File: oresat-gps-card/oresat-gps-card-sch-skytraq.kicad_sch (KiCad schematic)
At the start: 11 parts, among them U23 ORION-B16

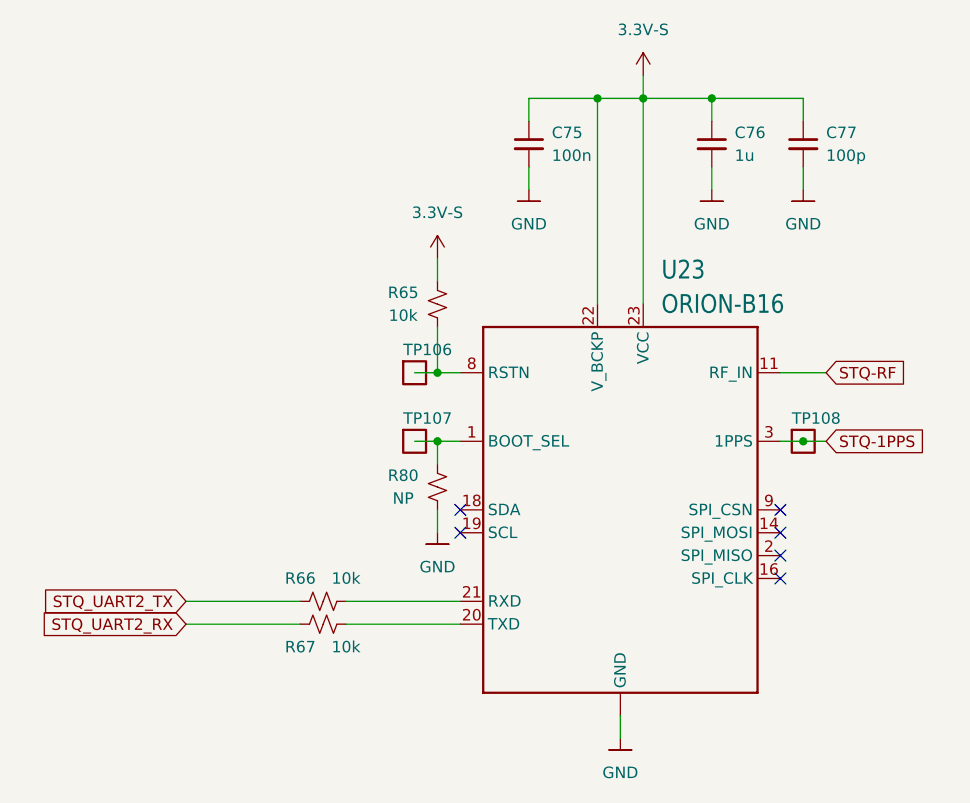
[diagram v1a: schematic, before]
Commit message: Quick GPS card design review changes
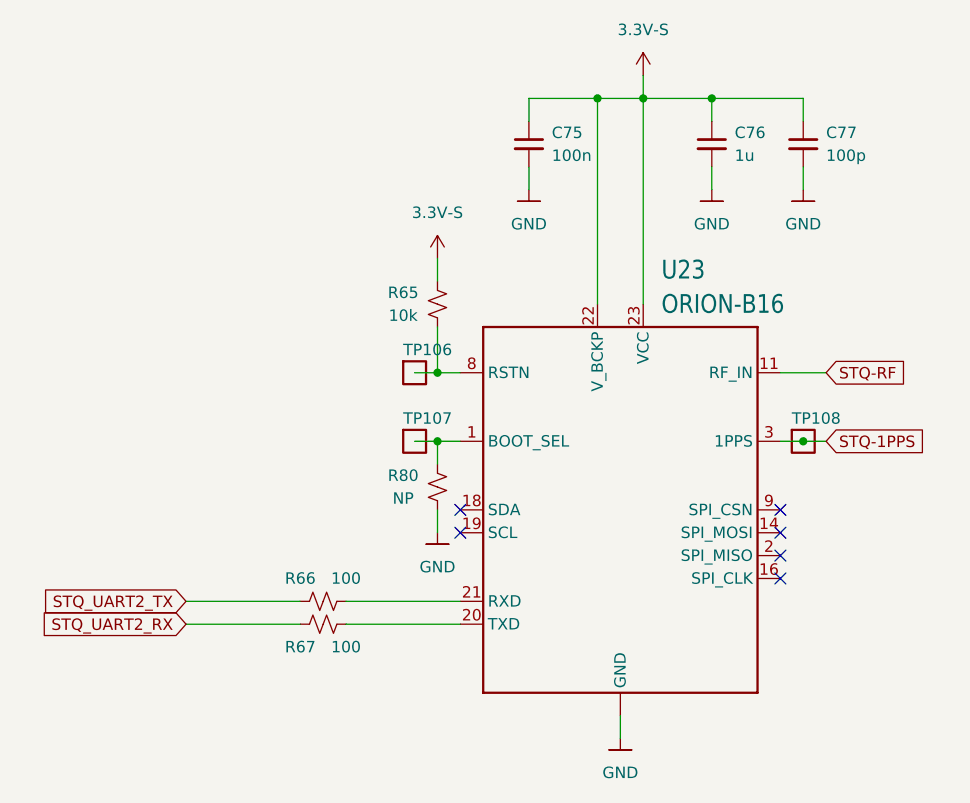
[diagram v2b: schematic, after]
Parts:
- R66, R67: value 10k -> 100
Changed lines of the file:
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@@
   (symbol (lib_id "OreSat-Power:GND") (at 226.06 99.06 0) (unit 1)
     (in_bom yes) (on_board yes) (fields_autoplaced)
-    (property "Reference" "#GND?" (id 0) (at 226.06 105.41 0)
+    (property "Reference" "#GND0222" (id 0) (at 226.06 105.41 0)
       (effects (font (size 1.27 1.27)) hide)
     )
@@
   (symbol (lib_id "OreSat-Power:GND") (at 205.74 99.06 0) (unit 1)
     (in_bom yes) (on_board yes) (fields_autoplaced)
-    (property "Reference" "#GND?" (id 0) (at 205.74 105.41 0)
+    (property "Reference" "#GND0221" (id 0) (at 205.74 105.41 0)
       (effects (font (size 1.27 1.27)) hide)
     )
@@
   (symbol (lib_id "OreSat-Power:GND") (at 215.9 160.02 0) (unit 1)
     (in_bom yes) (on_board yes) (fields_autoplaced)
-    (property "Reference" "#GND?" (id 0) (at 215.9 166.37 0)
+    (property "Reference" "#GND0225" (id 0) (at 215.9 166.37 0)
       (effects (font (size 1.27 1.27)) hide)
     )
@@
     (in_bom yes) (on_board yes)
     (property "Reference" "R67" (id 0) (at 180.34 149.86 90))
-    (property "Value" "10k" (id 1) (at 185.42 149.86 90))
+    (property "Value" "100" (id 1) (at 185.42 149.86 90))
     (property "Footprint" "Resistor_SMD:R_0603_1608Metric" (id 2) (at 182.88 147.32 0)
       (effects (font (size 1.27 1.27)) hide)
@@
   (symbol (lib_id "gps-power:3.3V-S") (at 218.44 86.36 0) (unit 1)
     (in_bom no) (on_board no) (fields_autoplaced)
-    (property "Reference" "#3V3-S?" (id 0) (at 218.44 81.28 0)
+    (property "Reference" "#3V3-S0102" (id 0) (at 218.44 81.28 0)
       (effects (font (size 1.27 1.27)) hide)
     )
@@
   (symbol (lib_id "OreSat-Power:GND") (at 195.58 137.16 0) (unit 1)
     (in_bom yes) (on_board yes) (fields_autoplaced)
-    (property "Reference" "#GND?" (id 0) (at 195.58 143.51 0)
+    (property "Reference" "#GND0224" (id 0) (at 195.58 143.51 0)
       (effects (font (size 1.27 1.27)) hide)
     )
@@
     (in_bom yes) (on_board yes)
     (property "Reference" "R66" (id 0) (at 180.34 142.24 90))
-    (property "Value" "10k" (id 1) (at 185.42 142.24 90))
+    (property "Value" "100" (id 1) (at 185.42 142.24 90))
     (property "Footprint" "Resistor_SMD:R_0603_1608Metric" (id 2) (at 182.88 144.78 0)
       (effects (font (size 1.27 1.27)) hide)
@@
   (symbol (lib_id "OreSat-Power:GND") (at 236.22 99.06 0) (unit 1)
     (in_bom yes) (on_board yes) (fields_autoplaced)
-    (property "Reference" "#GND?" (id 0) (at 236.22 105.41 0)
+    (property "Reference" "#GND0223" (id 0) (at 236.22 105.41 0)
       (effects (font (size 1.27 1.27)) hide)
     )
@@
   (symbol (lib_id "gps-power:3.3V-S") (at 195.58 106.68 0) (unit 1)
     (in_bom no) (on_board no) (fields_autoplaced)
-    (property "Reference" "#3V3-S?" (id 0) (at 195.58 101.6 0)
-      (effects (font (size 1.27 1.27)) hide)
-    )
+    (property "Reference" "#3V3-S0103" (id 0) (at 195.58 101.6 0)
+      (effects (font (size 1.27 1.27)) hide)
+    )

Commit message: Updated GPS card with changes from C3 and notes. Fixed library issues
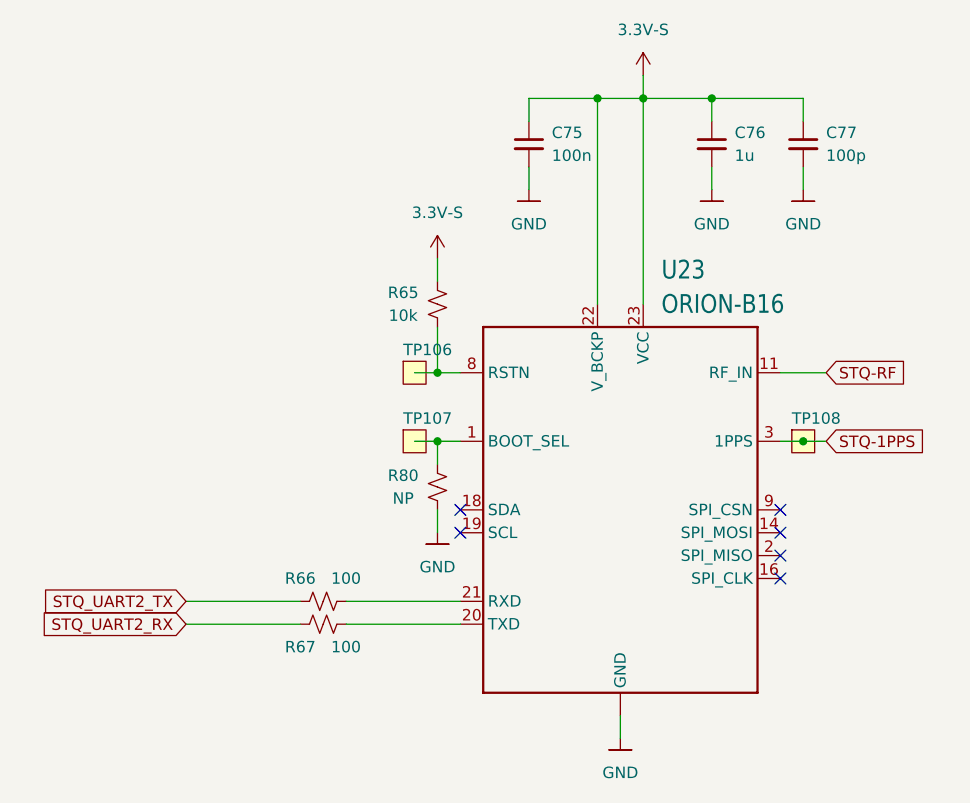
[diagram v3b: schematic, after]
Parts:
- TP106, TP107, TP108: value Test-Point -> 1x01; footprint OreSat-TestPoint:1X01 -> oresat-misc:TestPoint-0.75mm-th; symbol OreSat-TestPoint:Test-Point -> oresat-misc:Test-Point-0.75mm-th
- U23: symbol U-SkyTraq-ORION-B16-gps-receiver:ORION-B16 -> oresat-ics:ORION-B16

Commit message: Cleaned up ERC and DRC errors on GPS card
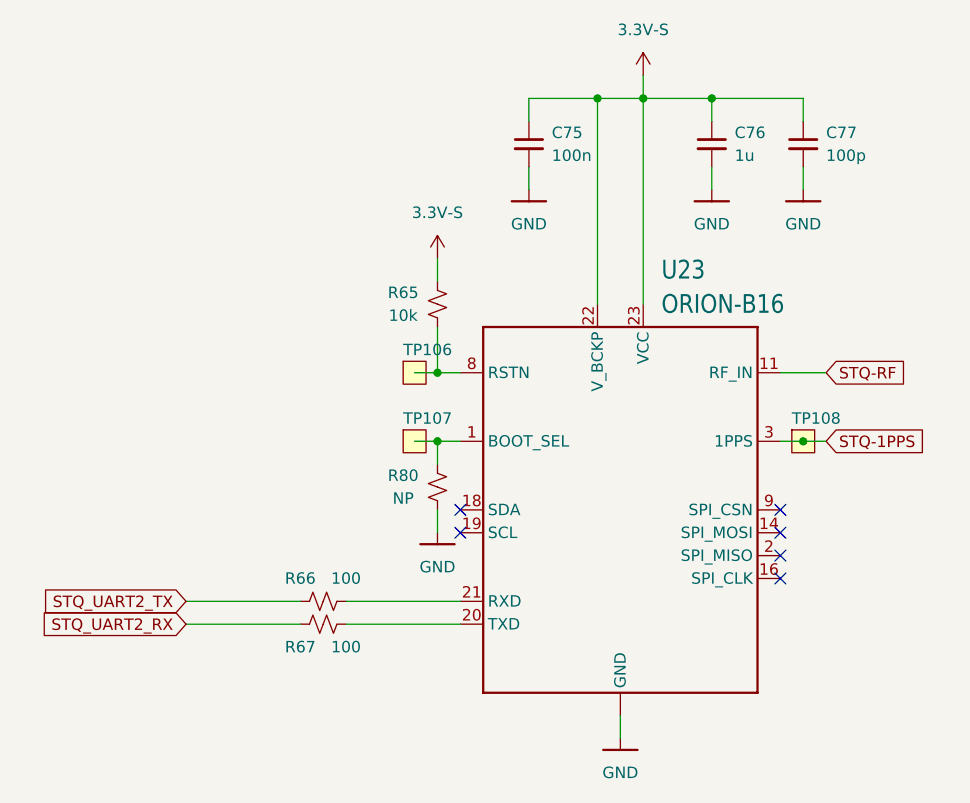
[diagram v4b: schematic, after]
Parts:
- U23: footprint oresat-footprints:U-SkyTraq-ORION-B16 -> oresat-ics:U-SkyTraq-ORION-B16
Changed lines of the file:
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@@
       (effects (font (size 2.0828 1.7703)) (justify left))
     )
-    (property "Footprint" "oresat-footprints:U-SkyTraq-ORION-B16" (at 215.9 134.62 0)
+    (property "Footprint" "oresat-ics:U-SkyTraq-ORION-B16" (at 215.9 134.62 0)
       (effects (font (size 1.27 1.27)) hide)
     )

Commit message: Updated KiCAD 8, updated schematic sheet info, polished some schematic things, and made DNP parts DNP.
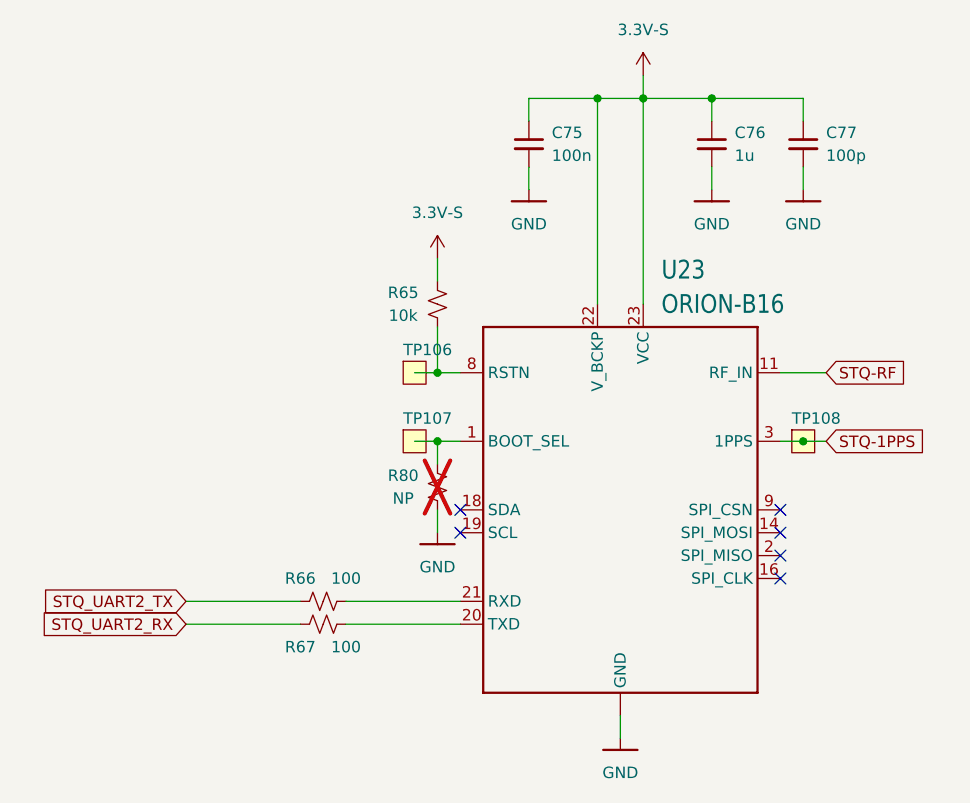
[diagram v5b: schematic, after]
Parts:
- R80: now not fitted; now left out of the parts list
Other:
- title: (none) -> OreSat GPS Card

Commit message: updated symbols and started new 2771 symbol
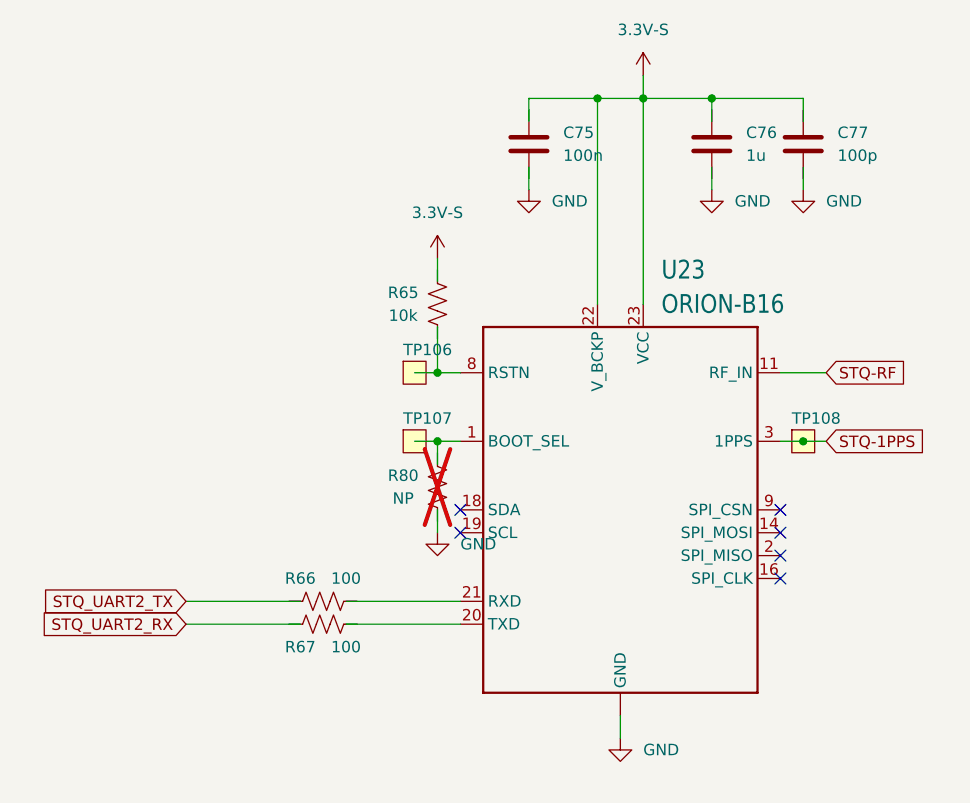
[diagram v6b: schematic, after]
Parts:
- C75, C76, C77: symbol Device:C_Small -> Device:C
- R65, R66, R67: symbol Device:R_Small_US -> Device:R_US
- R80: symbol Device:R_Small_US -> Device:R_US; now in the parts list
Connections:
- net 3.3V-S: no longer C75.1, C76.1, C77.1, R65.1
- net GND: no longer C75.2, C76.2, C77.2, R80.2
- net STQ_UART2_RX: no longer R67.1
- net STQ_UART2_TX: no longer R66.1
- net at TP106.1, U23.8 (RSTN): no longer R65.2
- net at TP107.1, U23.1 (BOOT_SEL): no longer R80.1
- net at R67.2: no longer U23.20 (TXD)
- net at U23.21 (RXD): no longer R66.2
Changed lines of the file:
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@@
 (kicad_sch
-	(version 20231120)
+	(version 20250114)
 	(generator "eeschema")
-	(generator_version "8.0")
+	(generator_version "9.0")
 	(paper "B")
 	(title_block
@@
 	)
 	(symbol
-		(lib_id "oresat-power:GND")
+		(lib_id "power:GND")
 		(at 226.06 99.06 0)
 		(unit 1)
@@
 		)
 		(property "Value" "GND"
-			(at 226.06 102.87 0)
-			(effects
-				(font
-					(size 1.27 1.27)
-				)
+			(at 228.6 100.3299 0)
+			(effects
+				(font
+					(size 1.27 1.27)
+				)
+				(justify left)
 			)
 		)
@@
 			)
 		)
-		(property "Description" ""
+		(property "Description" "Power symbol creates a global label with name \"GND\" , ground"
 			(at 226.06 99.06 0)
 			(effects
@@
 	)
 	(symbol
-		(lib_id "oresat-power:GND")
+		(lib_id "power:GND")
 		(at 205.74 99.06 0)
 		(unit 1)
@@
 		)
 		(property "Value" "GND"
-			(at 205.74 102.87 0)
-			(effects
-				(font
-					(size 1.27 1.27)
-				)
+			(at 208.28 100.3299 0)
+			(effects
+				(font
+					(size 1.27 1.27)
+				)
+				(justify left)
 			)
 		)
@@
 			)
 		)
-		(property "Description" ""
+		(property "Description" "Power symbol creates a global label with name \"GND\" , ground"
 			(at 205.74 99.06 0)
 			(effects
@@
 	)
 	(symbol
-		(lib_id "Device:R_Small_US")
+		(lib_id "Device:R_US")
 		(at 195.58 111.76 0)
 		(unit 1)
@@
 		)
 		(property "Footprint" "Resistor_SMD:R_0603_1608Metric"
-			(at 195.58 111.76 0)
+			(at 196.596 112.014 90)
 			(effects
 				(font
@@
 			)
 		)
-		(property "Description" ""
+		(property "Description" "Resistor, US symbol"
 			(at 195.58 111.76 0)
 			(effects
@@
 	)
 	(symbol
-		(lib_id "Device:C_Small")
+		(lib_id "Device:C")
 		(at 226.06 93.98 0)
 		(unit 1)
@@
 		(fields_autoplaced yes)
 		(property "Reference" "C76"
-			(at 228.6 92.7162 0)
+			(at 229.87 92.7099 0)
 			(effects
 				(font
@@
 		)
 		(property "Value" "1u"
-			(at 228.6 95.2562 0)
+			(at 229.87 95.2499 0)
 			(effects
 				(font
@@
 		)
 		(property "Footprint" "Capacitor_SMD:C_0603_1608Metric"
-			(at 226.06 93.98 0)
+			(at 227.0252 97.79 0)
 			(effects
 				(font
@@
 			)
 		)
-		(property "Description" ""
+		(property "Description" "Unpolarized capacitor"
 			(at 226.06 93.98 0)
 			(effects
@@
 	)
 	(symbol
-		(lib_id "oresat-power:GND")
+		(lib_id "power:GND")
 		(at 215.9 160.02 0)
 		(unit 1)
@@
 		)
 		(property "Value" "GND"
-			(at 215.9 163.83 0)
-			(effects
-				(font
-					(size 1.27 1.27)
-				)
+			(at 218.44 161.2899 0)
+			(effects
+				(font
+					(size 1.27 1.27)
+				)
+				(justify left)
 			)
 		)
@@
 			)
 		)
-		(property "Description" ""
+		(property "Description" "Power symbol creates a global label with name \"GND\" , ground"
 			(at 215.9 160.02 0)
 			(effects
@@
 	)
 	(symbol
-		(lib_id "Device:C_Small")
+		(lib_id "Device:C")
 		(at 205.74 93.98 0)
 		(unit 1)
@@
 		(fields_autoplaced yes)
 		(property "Reference" "C75"
-			(at 208.28 92.7162 0)
+			(at 209.55 92.7099 0)
 			(effects
 				(font
@@
 		)
 		(property "Value" "100n"
-			(at 208.28 95.2562 0)
+			(at 209.55 95.2499 0)
 			(effects
 				(font
@@
 		)
 		(property "Footprint" "Capacitor_SMD:C_0603_1608Metric"
-			(at 205.74 93.98 0)
+			(at 206.7052 97.79 0)
 			(effects
 				(font
@@
 			)
 		)
-		(property "Description" ""
+		(property "Description" "Unpolarized capacitor"
 			(at 205.74 93.98 0)
 			(effects
@@
 	)
 	(symbol
-		(lib_id "Device:R_Small_US")
+		(lib_id "Device:R_US")
 		(at 182.88 147.32 90)
 		(unit 1)
@@
 		)
 		(property "Footprint" "Resistor_SMD:R_0603_1608Metric"
-			(at 182.88 147.32 0)
+			(at 183.134 146.304 90)
 			(effects
 				(font
@@
 			)
 		)
-		(property "Description" ""
+		(property "Description" "Resistor, US symbol"
 			(at 182.88 147.32 0)
 			(effects
@@
 	)
 	(symbol
-		(lib_id "Device:C_Small")
+		(lib_id "Device:C")
 		(at 236.22 93.98 0)
 		(unit 1)
@@
 		(fields_autoplaced yes)
 		(property "Reference" "C77"
-			(at 238.76 92.7162 0)
+			(at 240.03 92.7099 0)
 			(effects
 				(font
@@
 		)
 		(property "Value" "100p"
-			(at 238.76 95.2562 0)
+			(at 240.03 95.2499 0)
 			(effects
 				(font
@@
 		)
 		(property "Footprint" "Capacitor_SMD:C_0603_1608Metric"
-			(at 236.22 93.98 0)
+			(at 237.1852 97.79 0)
 			(effects
 				(font
@@
 			)
 		)
-		(property "Description" ""
+		(property "Description" "Unpolarized capacitor"
 			(at 236.22 93.98 0)
 			(effects
@@
 	)
 	(symbol
-		(lib_id "oresat-power:GND")
+		(lib_id "power:GND")
 		(at 195.58 137.16 0)
 		(unit 1)
@@
 		)
 		(property "Value" "GND"
-			(at 195.58 140.97 0)
-			(effects
-				(font
-					(size 1.27 1.27)
-				)
+			(at 198.12 138.4299 0)
+			(effects
+				(font
+					(size 1.27 1.27)
+				)
+				(justify left)
 			)
 		)
@@
 			)
 		)
-		(property "Description" ""
+		(property "Description" "Power symbol creates a global label with name \"GND\" , ground"
 			(at 195.58 137.16 0)
 			(effects
@@
 	)
 	(symbol
-		(lib_id "Device:R_Small_US")
+		(lib_id "Device:R_US")
 		(at 182.88 144.78 90)
 		(unit 1)
@@
 		)
 		(property "Footprint" "Resistor_SMD:R_0603_1608Metric"
-			(at 182.88 144.78 0)
+			(at 183.134 143.764 90)
 			(effects
 				(font
@@
 			)
 		)
-		(property "Description" ""
+		(property "Description" "Resistor, US symbol"
 			(at 182.88 144.78 0)
 			(effects
@@
 	)
 	(symbol
-		(lib_id "oresat-power:GND")
+		(lib_id "power:GND")
 		(at 236.22 99.06 0)
 		(unit 1)
@@
 		)
 		(property "Value" "GND"
-			(at 236.22 102.87 0)
-			(effects
-				(font
-					(size 1.27 1.27)
-				)
+			(at 238.76 100.3299 0)
+			(effects
+				(font
+					(size 1.27 1.27)
+				)
+				(justify left)
 			)
 		)
@@
 			)
 		)
-		(property "Description" ""
+		(property "Description" "Power symbol creates a global label with name \"GND\" , ground"
 			(at 236.22 99.06 0)
 			(effects
@@
 	)
 	(symbol
-		(lib_id "Device:R_Small_US")
+		(lib_id "Device:R_US")
 		(at 195.58 132.08 0)
 		(unit 1)
 		(exclude_from_sim no)
-		(in_bom no)
+		(in_bom yes)
 		(on_board yes)
 		(dnp yes)
@@
 		)
 		(property "Footprint" "Resistor_SMD:R_0603_1608Metric"
-			(at 195.58 132.08 0)
+			(at 196.596 132.334 90)
 			(effects
 				(font
@@
 			)
 		)
-		(property "Description" ""
+		(property "Description" "Resistor, US symbol"
 			(at 195.58 132.08 0)
 			(effects

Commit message: Routine Push
Various small changes made
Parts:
- removed TP106, TP107, TP108: 1x01, oresat-misc:TestPoint-0.75mm-th, symbol oresat-misc:Test-Point-0.75mm-th
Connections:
- net 3.3V-S: now also C75.1, C76.1, C77.1
- net GND: now also C75.2, C76.2, C77.2
- net at U23.8 (RSTN): now also R65.2
